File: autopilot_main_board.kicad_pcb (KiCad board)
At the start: 4 copper layers, 139 parts, among them J1 Conn_01x05, J10 Screw_Terminal_01x02, J2 Conn_ARM_JTAG_SWD_10, J3 Conn_02x06_Row_Letter_Last, J4 Conn_01x04, J5 Screw_Terminal_01x03, J6 Conn_01x05_Pin, J8 Conn_01x02_Socket, J9 Conn_01x02_Socket, Q1 SIR182DP-T1-RE3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

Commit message: Initial PCB layout
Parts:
- added FM1: ~, Fiducial:Fiducial_1mm_Mask2mm, F.Cu at (110.8, 123.5)
- added FM2: ~, Fiducial:Fiducial_1mm_Mask2mm, F.Cu at (110.8, 73.5)
- added FM3: ~, Fiducial:Fiducial_1mm_Mask2mm, F.Cu at (199.8, 73.5)
- J3: value Conn_02x06_Row_Letter_Last -> Conn_02x06_Top_Bottom
- J6: footprint Connector_JST:JST_PH_B4B-PH-K_1x04_P2.00mm_Vertical -> Connector_JST:JST_XH_B5B-XH-AM_1x05_P2.50mm_Vertical
- L1: footprint Inductor_SMD:L_0603_1608Metric -> Inductor_SMD:L_1206_3216Metric
- U3: footprint RF_Module:ESP32-C6-MINI-1 -> 1_SOC:ESP32-C6-MINI-1
- moved J5 173.6 mm to (204.8, 113.5), turned to 90 degrees
- moved J10 148.6 mm to (204.8, 87.5), turned to 90 degrees
- moved J1 141.7 mm to (184.3, 72.5)
- moved C1 123.7 mm to (198.8, 79.5), turned to -90 degrees
- moved C6 118.5 mm to (196.2, 85.5), turned to 90 degrees
- moved R36 118.4 mm to (182.8, 111.5), turned to 180 degrees
- moved Q3 117.8 mm to (192.8, 109.5)
- moved R38 117.7 mm to (186.5, 111.5)
- moved C5 116.0 mm to (192.8, 85.5), turned to 90 degrees
- moved D1 115.7 mm to (196.1, 79.5), turned to 90 degrees
- moved C2 115.6 mm to (191.3, 79.4), turned to -90 degrees
- moved C27 114.6 mm to (185.3, 120.5), turned to 180 degrees
- moved C4 113.6 mm to (189.5, 85.5), turned to 90 degrees
- moved R41 112.6 mm to (172.8, 125.5), turned to 90 degrees
- moved R1 111.5 mm to (193.8, 78.7), turned to 90 degrees
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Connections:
- net /ESP32-C6/EN renamed /ESP32/EN
- net /ESP32-C6/NRST renamed /Connectors/NRST
- net /ESP32-C6/RX renamed /ESP32/RX
- net /ESP32-C6/TX renamed /ESP32/TX
- net /IMU/SCL renamed /Connectors/SCL
- net /IMU/SDA renamed /Connectors/SDA
- net /can/CAN_RX renamed /NMEA2000/CAN_RX
- net /can/CAN_TX renamed /NMEA2000/CAN_TX
- net /can/NMEA2000_V+ renamed /Connectors/NMEA2000_V+
- net /external_connectors/HALL1 renamed /Connectors/HALL1
- net /external_connectors/HALL2 renamed /Connectors/HALL2
- net /external_connectors/HALL3 renamed /Connectors/HALL3
- net /external_connectors/SWCLK renamed /Connectors/SWCLK
- net /external_connectors/SWDIO renamed /Connectors/SWDIO
- net /external_connectors/SWO renamed /Connectors/SWO
- net Net-(U4-CAP) renamed /IMU/CAP
- C25 pad 2: /can/NMEA2000_GND -> /Connectors/NMEA2000_GND
- J3 pad 1: (no net) -> VDD
- J3 pad 10: (no net) -> GND
- J3 pad 11: (no net) -> EXT_PC15
- J3 pad 12: (no net) -> GND
- J3 pad 2: (no net) -> GND
- J3 pad 3: (no net) -> EXT_PD2
- J3 pad 4: (no net) -> GND
- J3 pad 5: (no net) -> EXT_PB10
- J3 pad 6: (no net) -> GND
- J3 pad 7: (no net) -> EXT_PC13
- J3 pad 8: (no net) -> GND
- J3 pad 9: (no net) -> EXT_PC14
- J6 pad 3: /can/NMEA2000_GND -> /Connectors/NMEA2000_H
- J6 pad 4: /can/NMEA2000_H -> /Connectors/NMEA2000_L
- U2 pad 5: /can/NMEA2000_GND -> /Connectors/NMEA2000_GND
- U2 pad 6: /can/NMEA2000_L -> /Connectors/NMEA2000_L
- U2 pad 7: /can/NMEA2000_H -> /Connectors/NMEA2000_H
- U4 pad 1: (no net) -> unconnected-(U4-RESV_NC-Pad1)
- U4 pad 12: (no net) -> unconnected-(U4-RESV_NC-Pad12)
- U4 pad 13: (no net) -> unconnected-(U4-RESV_NC-Pad13)
- U4 pad 21: (no net) -> unconnected-(U4-RESV_NC-Pad21)
- U4 pad 22: (no net) -> unconnected-(U4-RESV_NC-Pad22)
- U4 pad 23: (no net) -> unconnected-(U4-RESV_NC-Pad23)
- U4 pad 24: (no net) -> unconnected-(U4-RESV_NC-Pad24)
- U4 pad 7: (no net) -> unconnected-(U4-RESV_NC-Pad7)
- U4 pad 8: (no net) -> unconnected-(U4-RESV_NC-Pad8)
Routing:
- net /current_sense_2/OPP: track 0.00 -> 18.1 mm
- net GND: track 0.00 -> 14.6 mm, vias 0 -> 1
- net /ESP32/EN: track 0.00 -> 13.5 mm
- net /current_sense_2/OPO: track 0.00 -> 13.1 mm
- net VREF+: track 0.00 -> 10.1 mm, vias 0 -> 2
- net /current_sense_2/OPN: track 0.00 -> 8.50 mm, vias 0 -> 2
- net /current_sense_2/Vshunt+: track 0.00 -> 1.03 mm, vias 0 -> 1
- added copper zone on F.Cu, net GND
- added copper zone on In1.Cu, net GND
- added copper zone on In2.Cu, net GND
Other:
- board outline added: 110 x 60 mm

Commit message: Continued routing
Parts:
- added C36: 10uF, Capacitor_SMD:C_1206_3216Metric, F.Cu at (104.9, 108.7)
- added C37: 100nF, Capacitor_SMD:C_1206_3216Metric, F.Cu at (104.9, 106.1)
- added FB1: BLM18PG601, Inductor_SMD:L_1206_3216Metric, F.Cu at (124.9, 125.0)
- C33: value 100n -> 10uF
- C34: value 100n -> 100nF
- moved R23 38.8 mm to (160.0, 98.2)
- moved C23 38.8 mm to (164.4, 97.4)
- moved D7 38.6 mm to (167.6, 97.3)
- moved R22 38.6 mm to (161.8, 98.2)
- moved C13 34.9 mm to (147.5, 83.7), turned to 90 degrees
- moved C16 32.4 mm to (152.4, 83.1)
- moved C18 32.4 mm to (152.4, 86.1)
- moved C33 30.6 mm to (122.2, 125.0), turned to 90 degrees
- moved U4 29.5 mm to (115.2, 122.2)
- moved C34 27.1 mm to (119.5, 125.0), turned to 90 degrees
- moved R57 18.0 mm to (119.6, 119.2), turned to 90 degrees
- moved C35 16.0 mm to (121.8, 118.4), turned to -90 degrees
- moved C15 15.3 mm to (153.5, 102.9)
- moved J3 13.7 mm to (143.0, 124.0)
- moved TP2 9.34 mm to (115.7, 106.2)
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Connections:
- C33 pad 1: VDD -> /IMU/VDD_IMU
- C34 pad 1: VDD -> /IMU/VDD_IMU
- R57 pad 1: VDD -> /IMU/VDD_IMU
- U4 pad 17: VDD -> /IMU/VDD_IMU
- U4 pad 28: VDD -> /IMU/VDD_IMU
- U4 pad 3: VDD -> /IMU/VDD_IMU
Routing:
- net VDD: track 0.00 -> 108.6 mm, vias 0 -> 2
- net /Connectors/SCL: track 0.00 -> 54.1 mm, vias 0 -> 2
- net /Connectors/SDA: track 0.00 -> 50.2 mm, vias 0 -> 2
- net /IMU/INTN: track 0.00 -> 48.2 mm, vias 0 -> 3
- net /IMU/NRST: track 0.00 -> 43.8 mm
- net /IMU/BOOTN: track 0.00 -> 38.9 mm
- net /Connectors/NRST: track 0.00 -> 30.2 mm
- net /NMEA2000/CAN_TX: track 0.00 -> 27.7 mm, vias 0 -> 2
- net /current_sense_1/OPP: track 0.00 -> 25.3 mm
- net /NMEA2000/CAN_RX: track 0.00 -> 24.8 mm
- net /current_sense_3/OPP: track 0.00 -> 23.4 mm
- net /Connectors/NMEA2000_GND: track 0.00 -> 20.9 mm
- net /current_sense_3/OPO: track 0.00 -> 20.8 mm
- net /current_sense_3/OPN: track 0.00 -> 20.3 mm
- net /current_sense_1/OPO: track 0.00 -> 19.2 mm
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- added copper zone on F.Cu, net Phase1
- added copper zone on F.Cu, net Phase2
- added copper zone on F.Cu, net Phase3
- added copper zone on B.Cu, net VM
- added copper zone on F.Cu, net VM
- removed copper zone on F.Cu, net GND

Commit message: Routing complete
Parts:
- moved TH1 54.5 mm to (123.1, 98.8)
- moved C21 54.4 mm to (123.0, 96.3)
- moved R21 54.2 mm to (123.9, 94.2)
- moved C13 23.8 mm to (159.2, 104.4), turned to 0 degrees
- moved R16 19.5 mm to (152.1, 117.4), turned to 90 degrees
- moved C7 19.2 mm to (157.2, 94.0)
- moved R17 16.7 mm to (153.8, 117.4), turned to 90 degrees
- moved C26 15.2 mm to (157.2, 97.0)
- moved D9 12.9 mm to (173.4, 125.4)
- moved R56 12.8 mm to (178.2, 126.2)
- moved C29 12.8 mm to (157.2, 100.3)
- moved C31 12.3 mm to (176.0, 125.4)
- moved R55 12.1 mm to (179.9, 126.2), turned to -90 degrees
- moved R54 10.4 mm to (181.7, 126.2), turned to 90 degrees
- moved C11 7.68 mm to (130.5, 91.7), turned to 0 degrees
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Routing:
- net VDD: track 108.6 -> 289.6 mm, vias 2 -> 9
- net Phase3: track 0.00 -> 102.1 mm, vias 0 -> 5
- net Phase2: track 0.00 -> 101.7 mm, vias 0 -> 3
- net Phase1: track 0.00 -> 90.5 mm, vias 0 -> 2
- net VM: track 0.00 -> 85.5 mm, vias 54 -> 55
- net /phase3/VPHASE: track 0.00 -> 83.8 mm, vias 0 -> 2
- net VREF+: track 19.1 -> 101.1 mm, vias 3 -> 7
- net VDDA: track 9.34 -> 87.2 mm, vias 0 -> 4
- net /current_sense_1/Vshunt+: track 0.00 -> 72.5 mm, vias 0 -> 4
- net /phase2/VPHASE: track 0.00 -> 70.2 mm, vias 0 -> 2
- net /Connectors/NRST: track 30.2 -> 94.7 mm, vias 0 -> 4
- net /ESP32/TX: track 0.00 -> 62.6 mm, vias 0 -> 2
- net /Connectors/HALL2: track 11.1 -> 72.0 mm, vias 0 -> 3
- net /phase1/GHS: track 0.00 -> 60.9 mm, vias 0 -> 2
- net /Connectors/HALL3: track 11.1 -> 71.7 mm, vias 0 -> 3
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- added copper zone on F.Cu, net /current_sense_1/Vshunt+
- added copper zone on F.Cu, net /current_sense_2/Vshunt+
- added copper zone on F.Cu, net /current_sense_3/Vshunt+
- added copper zone on B.Cu, net GND
- added copper zone on F.Cu, net GND

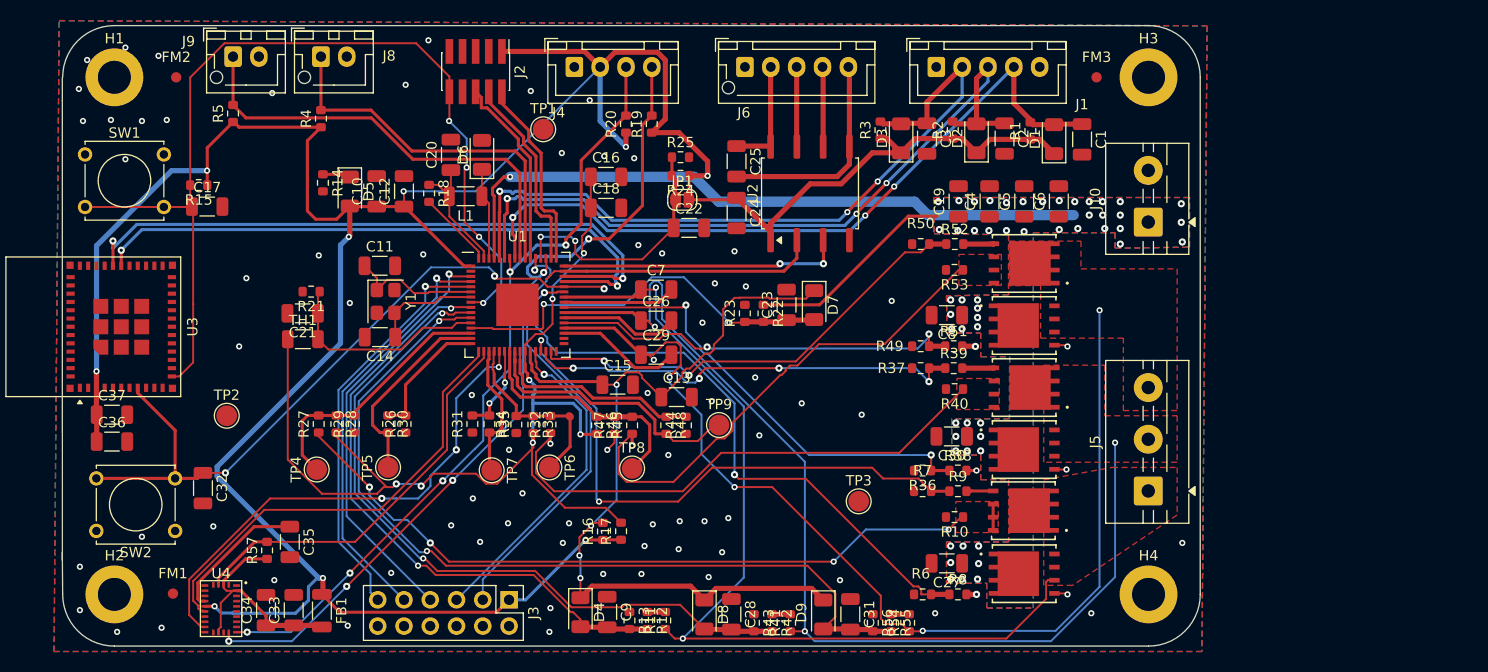
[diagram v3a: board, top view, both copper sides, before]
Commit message: DRC check completed
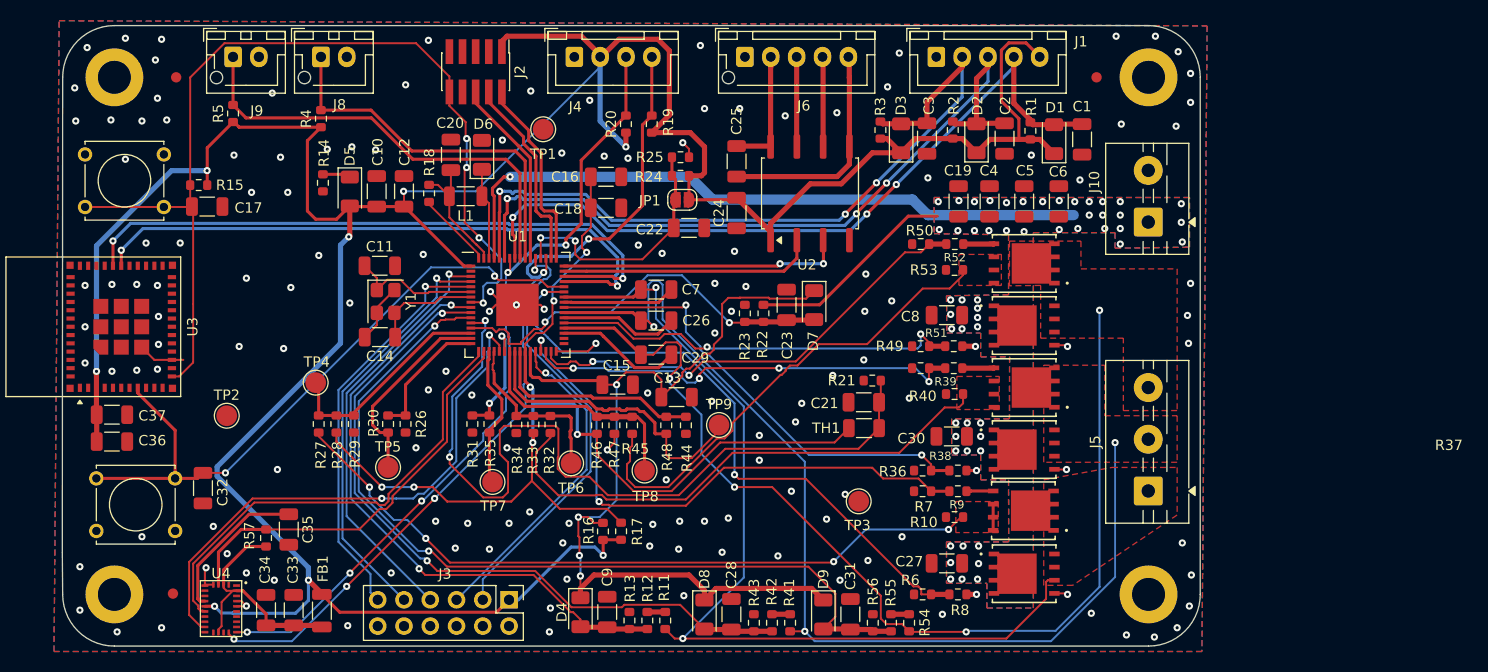
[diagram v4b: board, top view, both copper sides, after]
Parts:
- moved C21 54.9 mm to (177.3, 104.9)
- moved R21 54.9 mm to (178.1, 102.8)
- moved TH1 54.9 mm to (177.3, 107.4)
- moved TP4 8.40 mm to (124.3, 103.0)
- moved TP6 2.14 mm to (149.0, 110.8)
- moved TP8 1.22 mm to (156.1, 111.5)
- moved C35 1.20 mm to (121.7, 117.2)
- moved R57 1.20 mm to (119.5, 118.0)
- moved TP7 1.13 mm to (141.4, 112.6)
- moved J1 0.97 mm to (184.3, 71.5)
- moved J4 0.97 mm to (149.3, 71.5)
- moved J6 0.97 mm to (165.8, 71.5)
- moved R40 0.47 mm to (186.1, 104.1)
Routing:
- net /stspin32g4/Temp: track 20.9 -> 79.6 mm, vias 0 -> 2
- net GND: track 2.05 -> 31.9 mm, vias 71 -> 148
- net VDD: track 289.6 -> 307.3 mm, vias 9 -> 8
- net VREF+: track 101.1 -> 107.7 mm
- net VDDA: track 87.2 -> 93.2 mm
- net /NMEA2000/CAN_RX: track 29.1 -> 24.8 mm
- net /ESP32/EN: track 69.1 -> 64.9 mm, vias 3 -> 2
- net /current_sense_1/OPP: track 25.3 -> 21.5 mm
- net /IMU/INTN: track 49.0 -> 52.5 mm, vias 3 -> 2
- net /current_sense_2/OPN: track 8.54 -> 12.0 mm
- net /current_sense_3/OPO: track 26.8 -> 29.9 mm
- net /Connectors/HALL1: track 71.9 -> 73.9 mm
- net /Connectors/HALL3: track 71.7 -> 73.7 mm
- net /Connectors/HALL2: track 72.0 -> 74.0 mm
- net /Connectors/NMEA2000_V+: track 11.0 -> 13.0 mm
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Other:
- outline, holes or cut-outs redrawn
